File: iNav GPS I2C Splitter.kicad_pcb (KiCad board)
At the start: 2 copper layers, 34.5 x 16 mm, 3 parts

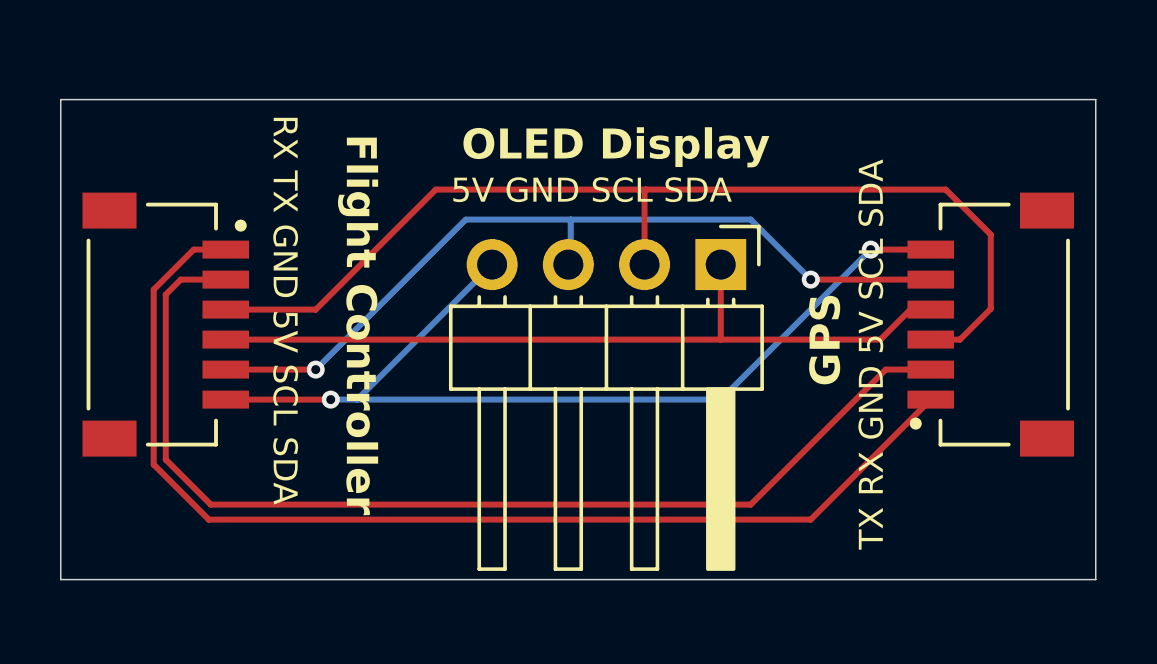
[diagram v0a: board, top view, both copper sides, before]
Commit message: Updated silkscreening for OLED pins
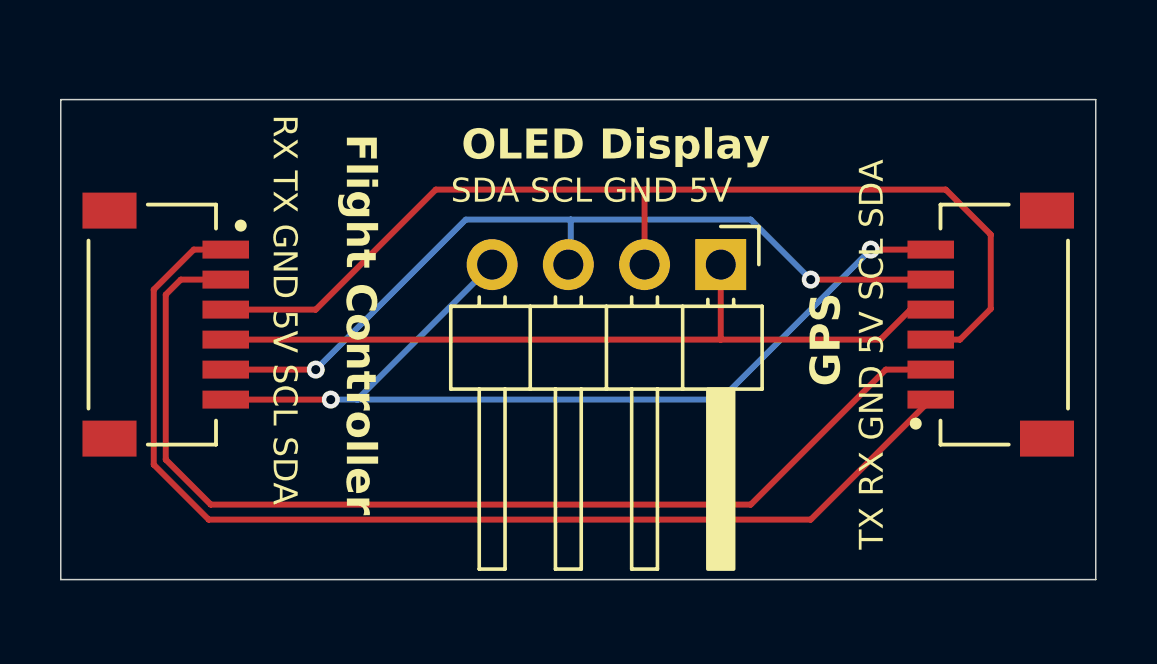
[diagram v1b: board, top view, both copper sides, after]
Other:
- board text added: "SDA SCL GND 5V"
- board text removed: "5V GND SCL SDA"
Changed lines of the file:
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@@
 		)
 	)
-	(gr_text "5V GND SCL SDA"
+	(gr_text "SDA SCL GND 5V"
 		(at 87 74 0)
 		(layer "F.SilkS")
